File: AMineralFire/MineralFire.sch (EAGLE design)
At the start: 76 parts, among them IC1 LM358, Q1 20MHz, Q2 20MHz, Q3 2N3906, Q4 2N3906, Q5 2N3906, Q6 2N3906, Q7 2N3906, Q8 2N3906, Q9 2N3906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

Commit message: Fixed up reset
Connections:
- new net RST2: ISP2.RST, U2.PC6(/RESET)
- net RST: no longer ISP2.RST, U2.PC6(/RESET)
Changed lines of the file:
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@@
 <label x="55.88" y="68.58" size="1.778" layer="95"/>
-</segment>
-<segment>
-<pinref part="U2" gate="G$1" pin="PC6(/RESET)"/>
-<wire x1="58.42" y1="233.68" x2="50.8" y2="233.68" width="0.1524" layer="91"/>
-<label x="50.8" y="233.68" size="1.778" layer="95"/>
-</segment>
-<segment>
-<pinref part="ISP2" gate="G$1" pin="RST"/>
-<wire x1="-7.62" y1="170.18" x2="-10.16" y2="170.18" width="0.1524" layer="91"/>
-<label x="-10.16" y="170.18" size="1.27" layer="95" rot="R180" xref="yes"/>
 </segment>
 </net>
@@
 </segment>
 </net>
+<net name="RST2" class="0">
+<segment>
+<pinref part="U2" gate="G$1" pin="PC6(/RESET)"/>
+<wire x1="58.42" y1="233.68" x2="50.8" y2="233.68" width="0.1524" layer="91"/>
+<label x="50.8" y="233.68" size="1.778" layer="95"/>
+</segment>
+<segment>
+<pinref part="ISP2" gate="G$1" pin="RST"/>
+<wire x1="-7.62" y1="170.18" x2="-10.16" y2="170.18" width="0.1524" layer="91"/>
+<label x="-10.16" y="170.18" size="1.27" layer="95" rot="R180" xref="yes"/>
+</segment>
+</net>

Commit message: Fixed RST on ISP2 and regulator was wrong way round
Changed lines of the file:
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@@
 <instance part="R11" gate="G$1" x="198.12" y="134.62" rot="R270"/>
 <instance part="R12" gate="G$1" x="187.96" y="134.62" rot="R270"/>
-<instance part="U3" gate="G$1" x="205.74" y="-7.62" rot="MR0"/>
+<instance part="U3" gate="G$1" x="205.74" y="-7.62"/>
 <instance part="C7" gate="G$1" x="220.98" y="-12.7"/>
 <instance part="SUPPLY10" gate="+5V" x="220.98" y="-2.54"/>
@@
 <pinref part="U3" gate="G$1" pin="IN"/>
 <wire x1="220.98" y1="-7.62" x2="220.98" y2="-10.16" width="0.1524" layer="91"/>
-<wire x1="213.36" y1="-7.62" x2="220.98" y2="-7.62" width="0.1524" layer="91"/>
+<wire x1="198.12" y1="-7.62" x2="220.98" y2="-7.62" width="0.1524" layer="91"/>
 <junction x="220.98" y="-7.62"/>
 </segment>
@@
 <pinref part="SUPPLY4" gate="+12V" pin="+12V"/>
 <pinref part="U3" gate="G$1" pin="OUT"/>
-<wire x1="182.88" y1="-7.62" x2="198.12" y2="-7.62" width="0.1524" layer="91"/>
+<wire x1="182.88" y1="-7.62" x2="213.36" y2="-7.62" width="0.1524" layer="91"/>
 <junction x="182.88" y="-7.62"/>
 </segment>
@@
 <segment>
 <pinref part="U2" gate="G$1" pin="PC6(/RESET)"/>
-<wire x1="58.42" y1="233.68" x2="50.8" y2="233.68" width="0.1524" layer="91"/>
-<label x="50.8" y="233.68" size="1.778" layer="95"/>
+<wire x1="58.42" y1="233.68" x2="53.34" y2="233.68" width="0.1524" layer="91"/>
+<label x="53.34" y="233.68" size="1.778" layer="95" rot="R180" xref="yes"/>
 </segment>
 <segment>
 <pinref part="ISP2" gate="G$1" pin="RST"/>
 <wire x1="-7.62" y1="170.18" x2="-10.16" y2="170.18" width="0.1524" layer="91"/>
-<label x="-10.16" y="170.18" size="1.27" layer="95" rot="R180" xref="yes"/>
-</segment>
-</net>
+<label x="-10.16" y="170.18" size="1.778" layer="95" rot="R180" xref="yes"/>
+</segment>
+</net>

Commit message: Fixed RST on ISP2 and regulator was wrong way round
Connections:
- net +12V: now also U3.IN; no longer U3.OUT
- net +5V: now also U3.OUT; no longer U3.IN
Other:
- moved on the sheet: U3
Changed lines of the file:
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@@
 <instance part="R11" gate="G$1" x="198.12" y="134.62" rot="R270"/>
 <instance part="R12" gate="G$1" x="187.96" y="134.62" rot="R270"/>
-<instance part="U3" gate="G$1" x="205.74" y="-7.62"/>
+<instance part="U3" gate="G$1" x="205.74" y="-7.62" rot="MR180"/>
 <instance part="C7" gate="G$1" x="220.98" y="-12.7"/>
 <instance part="SUPPLY10" gate="+5V" x="220.98" y="-2.54"/>
@@
 <pinref part="U3" gate="G$1" pin="GND"/>
 <wire x1="182.88" y1="-20.32" x2="205.74" y2="-20.32" width="0.1524" layer="91"/>
-<wire x1="205.74" y1="-20.32" x2="205.74" y2="-15.24" width="0.1524" layer="91"/>
+<wire x1="205.74" y1="-20.32" x2="205.74" y2="0" width="0.1524" layer="91"/>
 <junction x="182.88" y="-20.32"/>
 <pinref part="C7" gate="G$1" pin="-"/>
@@
 <pinref part="SUPPLY10" gate="+5V" pin="+5V"/>
 <wire x1="220.98" y1="-5.08" x2="220.98" y2="-7.62" width="0.1524" layer="91"/>
-<pinref part="U3" gate="G$1" pin="IN"/>
+<pinref part="U3" gate="G$1" pin="OUT"/>
 <wire x1="220.98" y1="-7.62" x2="220.98" y2="-10.16" width="0.1524" layer="91"/>
-<wire x1="198.12" y1="-7.62" x2="220.98" y2="-7.62" width="0.1524" layer="91"/>
+<wire x1="213.36" y1="-7.62" x2="220.98" y2="-7.62" width="0.1524" layer="91"/>
 <junction x="220.98" y="-7.62"/>
 </segment>
@@
 <junction x="172.72" y="-7.62"/>
 <pinref part="SUPPLY4" gate="+12V" pin="+12V"/>
-<pinref part="U3" gate="G$1" pin="OUT"/>
-<wire x1="182.88" y1="-7.62" x2="213.36" y2="-7.62" width="0.1524" layer="91"/>
+<pinref part="U3" gate="G$1" pin="IN"/>
+<wire x1="182.88" y1="-7.62" x2="198.12" y2="-7.62" width="0.1524" layer="91"/>
 <junction x="182.88" y="-7.62"/>
 </segment>

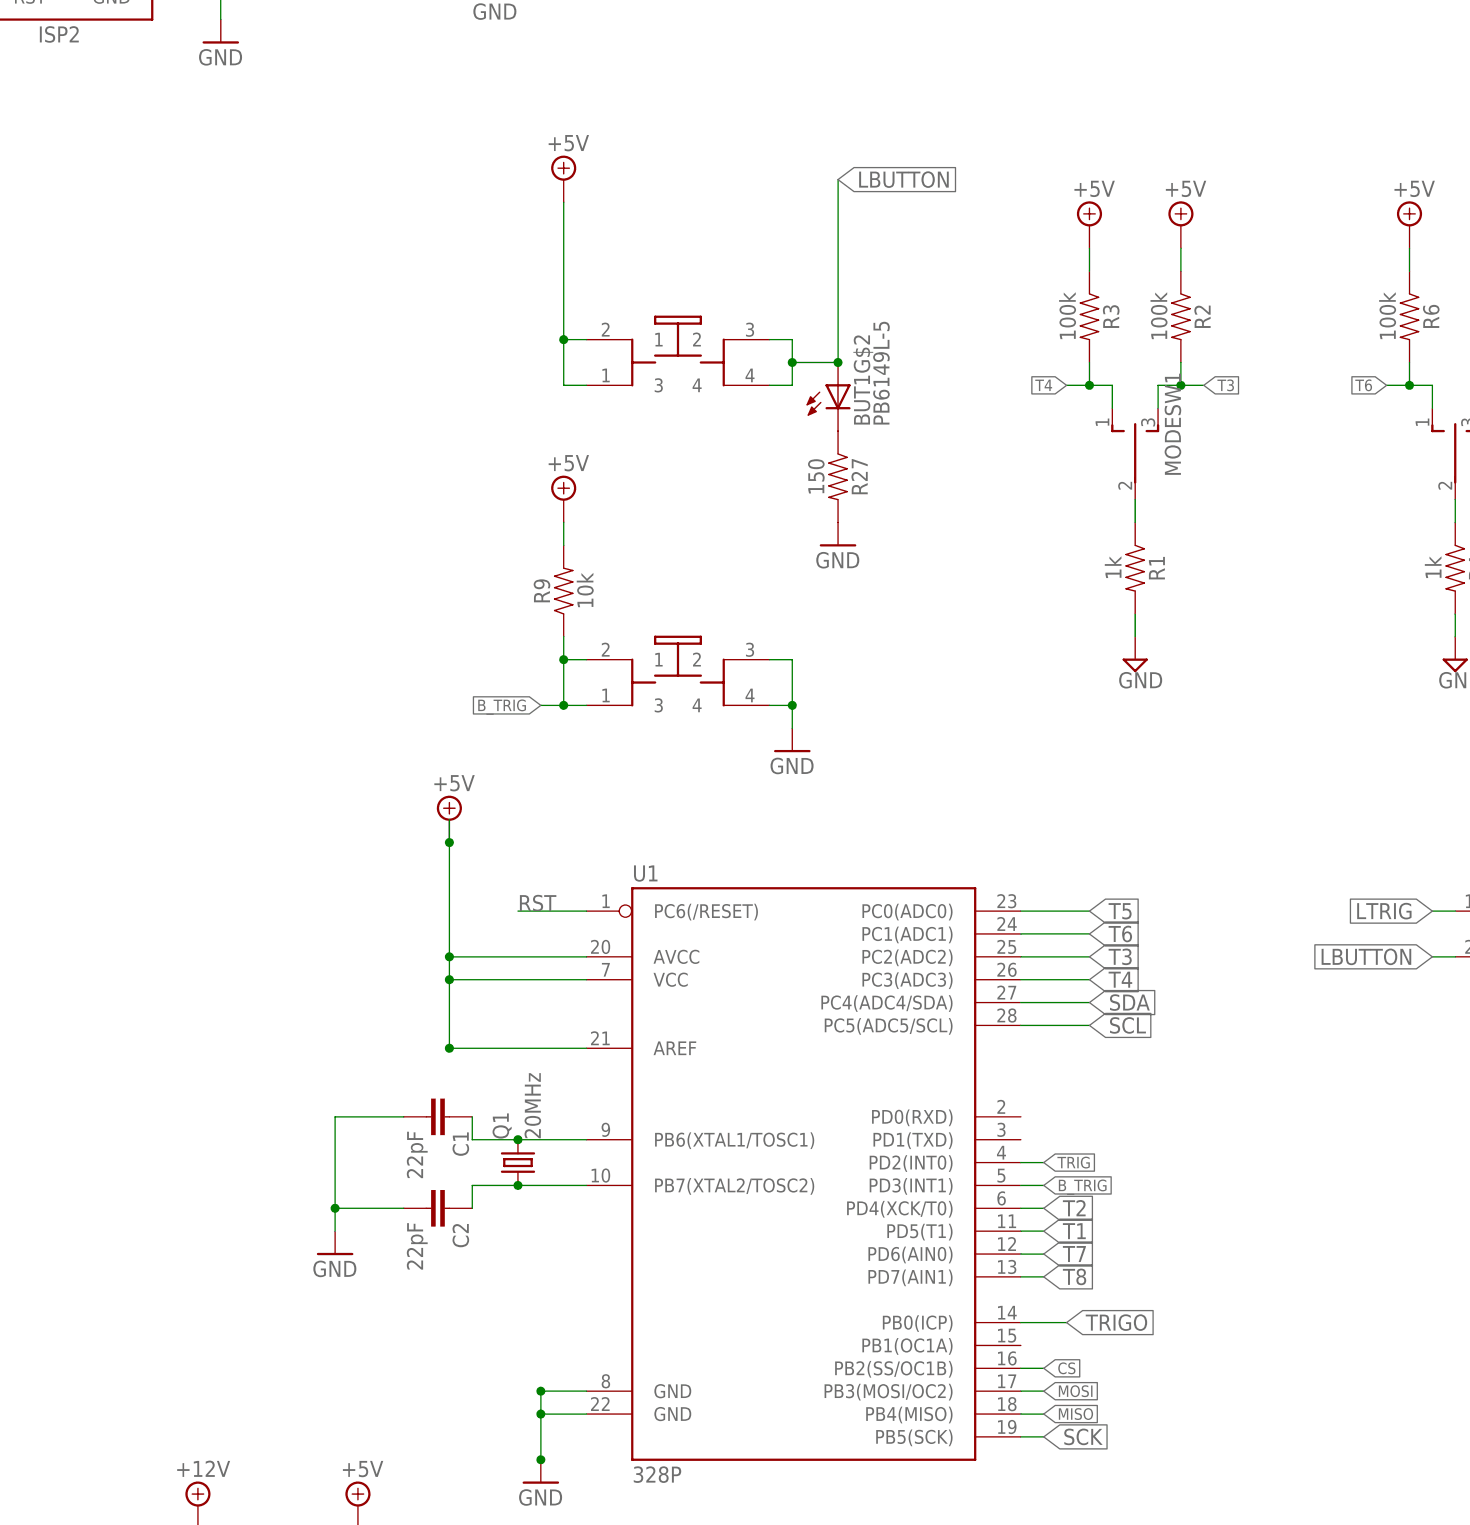
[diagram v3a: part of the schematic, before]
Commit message: changed push button
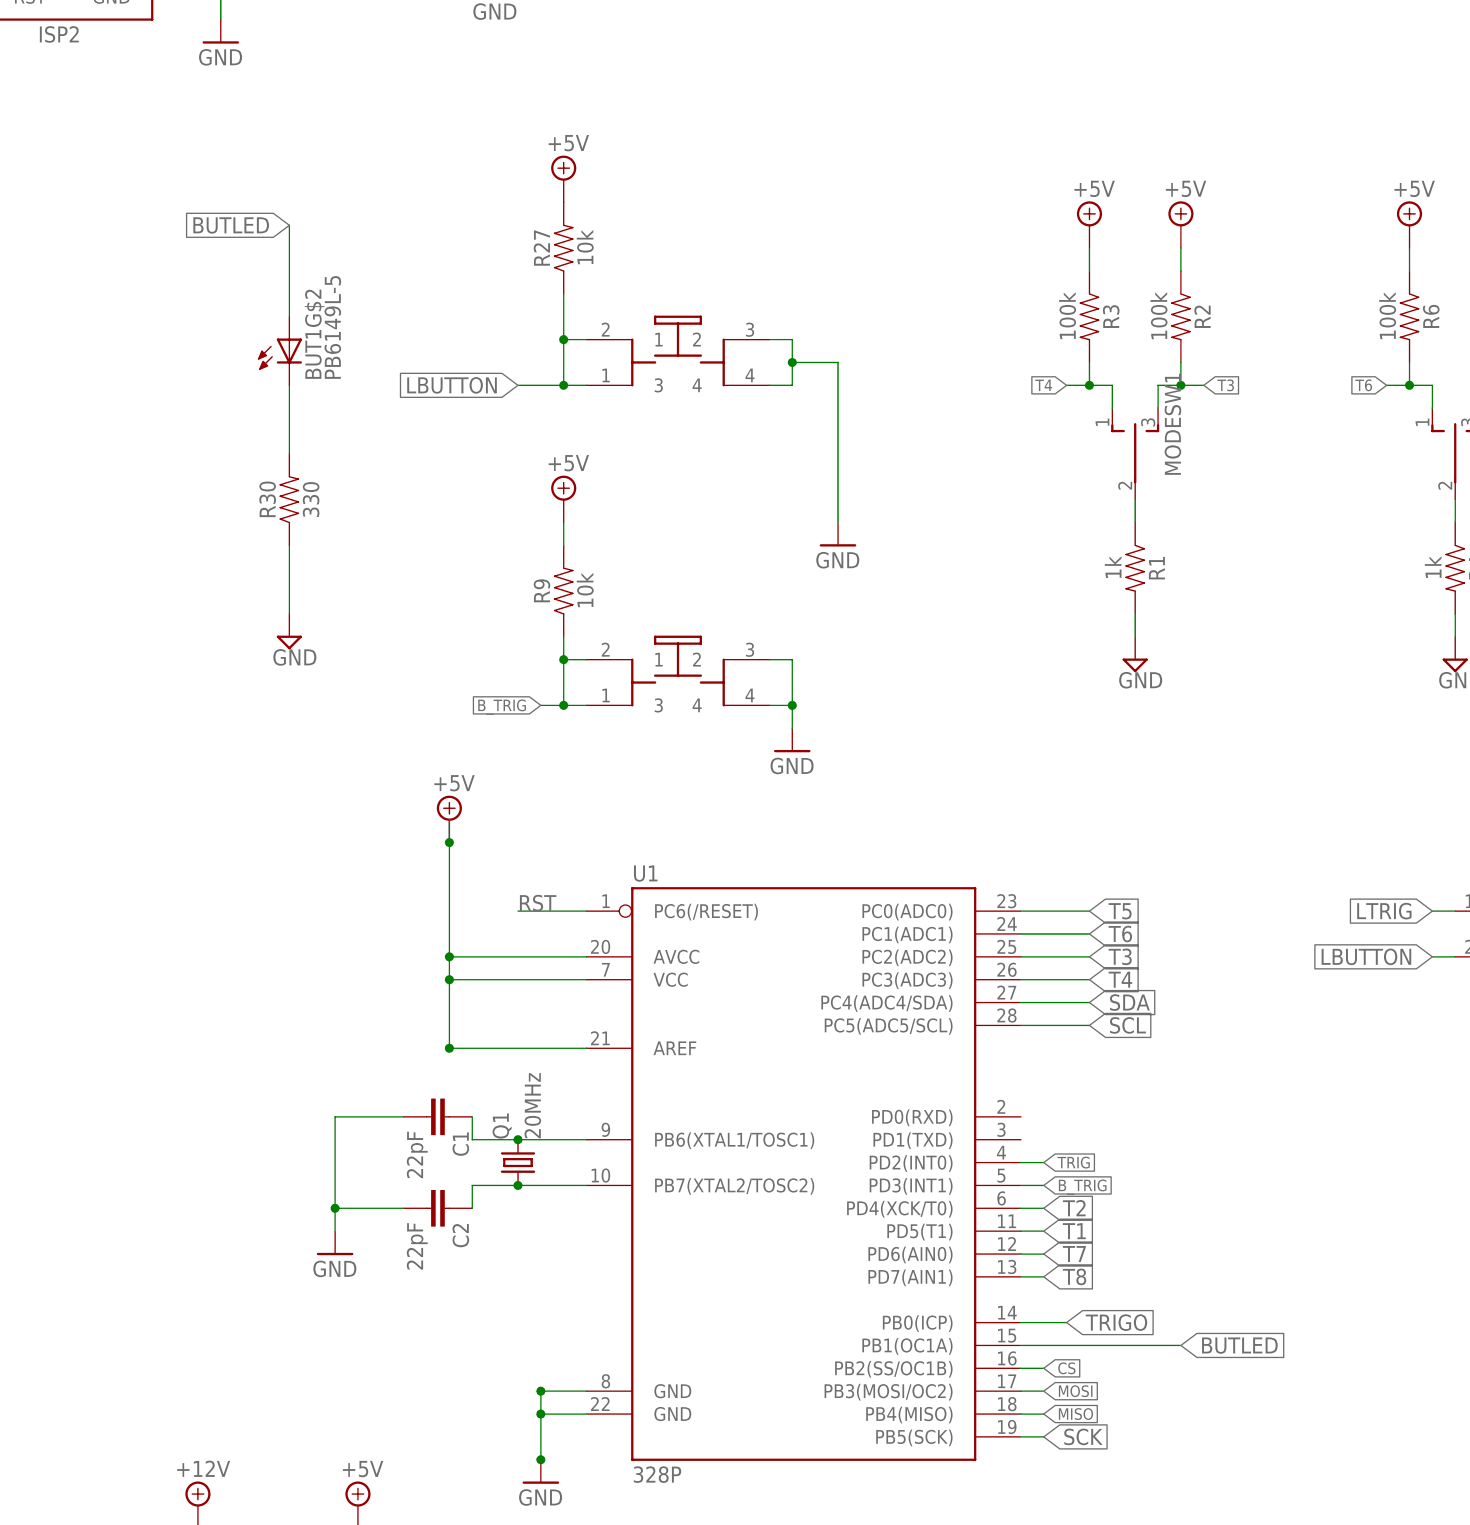
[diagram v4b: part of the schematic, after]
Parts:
- added R30: 330, SparkFun-Resistors:330OHM-HORIZ-1/10W-5%
- R27: value 150 -> 10k; device SparkFun-Resistors:100KOHM-HORIZ-1/4W-5% -> SparkFun-Resistors:10KOHM-HORIZ-1/4W-1%
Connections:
- new net BUTLED: BUT1G$2.A, U1.PB1(OC1A)
- net +5V: now also R27.2; no longer BUT1G$1.1, BUT1G$1.3
- net GND: now also BUT1G$1.2, BUT1G$1.4, R30.1; no longer R27.2
- net LBUTTON: now also BUT1G$1.1, BUT1G$1.3, R27.1; no longer BUT1G$1.2, BUT1G$1.4, BUT1G$2.A
- net N$19: now also R30.2; no longer R27.1
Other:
- moved on the sheet: BUT1G$2, R27
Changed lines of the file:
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@@
 <part name="BUT" library="INSTRUO" deviceset="PB6149L-5" device="" value="PB6149L-5"/>
 <part name="BUT1" library="INSTRUO" deviceset="PB6149L-5" device="" value="PB6149L-5"/>
-<part name="R27" library="SparkFun-Resistors" deviceset="100KOHM" device="-HORIZ-1/4W-5%" value="150"/>
 <part name="V1" library="74ttl-din" deviceset="74*32" device="N"/>
 <part name="SUPPLY28" library="supply2" deviceset="+5V" device=""/>
@@
 <part name="R28" library="SparkFun-Resistors" deviceset="100OHM" device="-HORIZ_KIT-1/4W-1%" value="100"/>
 <part name="R29" library="SparkFun-Resistors" deviceset="100OHM" device="-HORIZ_KIT-1/4W-1%" value="100"/>
+<part name="R27" library="SparkFun-Resistors" deviceset="10KOHM" device="-HORIZ-1/4W-1%" value="10k"/>
+<part name="R30" library="SparkFun-Resistors" deviceset="330OHM" device="-HORIZ-1/10W-5%" value="330"/>
+<part name="SUPPLY41" library="supply2" library_urn="urn:adsk.eagle:library:372" deviceset="GND" device=""/>
 </parts>
 <sheets>
@@
 <instance part="BUT" gate="G$2" x="256.54" y="17.78" rot="R90"/>
 <instance part="BUT1" gate="G$1" x="73.66" y="132.08"/>
-<instance part="BUT1" gate="G$2" x="91.44" y="127"/>
-<instance part="R27" gate="G$1" x="91.44" y="116.84" rot="R270"/>
+<instance part="BUT1" gate="G$2" x="30.48" y="132.08"/>
 <instance part="V1" gate="/1" x="170.18" y="66.04"/>
 <instance part="V1" gate="/+UB" x="203.2" y="73.66"/>
@@
 <instance part="R28" gate="G$1" x="426.72" y="195.58" rot="R90"/>
 <instance part="R29" gate="G$1" x="444.5" y="241.3" rot="R90"/>
+<instance part="R27" gate="G$1" x="60.96" y="142.24" rot="R90"/>
+<instance part="R30" gate="G$1" x="30.48" y="114.3" rot="R90"/>
+<instance part="SUPPLY41" gate="GND" x="30.48" y="99.06"/>
 </instances>
 <busses>
@@
 </segment>
 <segment>
-<pinref part="R27" gate="G$1" pin="2"/>
+<wire x1="83.82" y1="132.08" x2="86.36" y2="132.08" width="0.1524" layer="91"/>
+<wire x1="86.36" y1="132.08" x2="86.36" y2="129.54" width="0.1524" layer="91"/>
+<wire x1="86.36" y1="129.54" x2="86.36" y2="127" width="0.1524" layer="91"/>
+<wire x1="83.82" y1="127" x2="86.36" y2="127" width="0.1524" layer="91"/>
+<pinref part="BUT1" gate="G$1" pin="2"/>
+<pinref part="BUT1" gate="G$1" pin="4"/>
 <pinref part="GND5" gate="1" pin="GND"/>
+<wire x1="86.36" y1="129.54" x2="91.44" y2="129.54" width="0.1524" layer="91"/>
+<wire x1="91.44" y1="129.54" x2="91.44" y2="111.76" width="0.1524" layer="91"/>
+<junction x="86.36" y="129.54"/>
+</segment>
+<segment>
+<pinref part="R30" gate="G$1" pin="1"/>
+<wire x1="30.48" y1="109.22" x2="30.48" y2="101.6" width="0.1524" layer="91"/>
+<pinref part="SUPPLY41" gate="GND" pin="GND"/>
 </segment>
 </net>
@@
 </segment>
 <segment>
-<pinref part="SUPPLY27" gate="+5V" pin="+5V"/>
-<wire x1="60.96" y1="147.32" x2="60.96" y2="132.08" width="0.1524" layer="91"/>
-<wire x1="60.96" y1="132.08" x2="60.96" y2="127" width="0.1524" layer="91"/>
-<wire x1="63.5" y1="127" x2="60.96" y2="127" width="0.1524" layer="91"/>
-<pinref part="BUT1" gate="G$1" pin="3"/>
-<pinref part="BUT1" gate="G$1" pin="1"/>
-<wire x1="60.96" y1="132.08" x2="63.5" y2="132.08" width="0.1524" layer="91"/>
-<junction x="60.96" y="132.08"/>
-</segment>
-<segment>
 <pinref part="Q9" gate="G$1" pin="E"/>
 <wire x1="370.84" y1="294.64" x2="370.84" y2="299.72" width="0.1524" layer="91"/>
@@
 <wire x1="259.08" y1="233.68" x2="259.08" y2="238.76" width="0.1524" layer="91"/>
 <pinref part="SUPPLY40" gate="+5V" pin="+5V"/>
+</segment>
+<segment>
+<pinref part="SUPPLY27" gate="+5V" pin="+5V"/>
+<pinref part="R27" gate="G$1" pin="2"/>
 </segment>
 </net>
@@
 </segment>
 <segment>
-<wire x1="83.82" y1="132.08" x2="86.36" y2="132.08" width="0.1524" layer="91"/>
-<wire x1="86.36" y1="132.08" x2="86.36" y2="129.54" width="0.1524" layer="91"/>
-<wire x1="86.36" y1="129.54" x2="86.36" y2="127" width="0.1524" layer="91"/>
-<wire x1="83.82" y1="127" x2="86.36" y2="127" width="0.1524" layer="91"/>
-<pinref part="BUT1" gate="G$1" pin="2"/>
-<pinref part="BUT1" gate="G$1" pin="4"/>
-<wire x1="86.36" y1="129.54" x2="91.44" y2="129.54" width="0.1524" layer="91"/>
-<junction x="86.36" y="129.54"/>
-<pinref part="BUT1" gate="G$2" pin="A"/>
-<wire x1="91.44" y1="129.54" x2="91.44" y2="149.86" width="0.1524" layer="91"/>
-<junction x="91.44" y="129.54"/>
-<label x="91.44" y="149.86" size="1.778" layer="95" xref="yes"/>
+<pinref part="R27" gate="G$1" pin="1"/>
+<wire x1="60.96" y1="137.16" x2="60.96" y2="132.08" width="0.1524" layer="91"/>
+<pinref part="BUT1" gate="G$1" pin="1"/>
+<wire x1="60.96" y1="132.08" x2="63.5" y2="132.08" width="0.1524" layer="91"/>
+<wire x1="60.96" y1="132.08" x2="60.96" y2="127" width="0.1524" layer="91"/>
+<junction x="60.96" y="132.08"/>
+<pinref part="BUT1" gate="G$1" pin="3"/>
+<wire x1="60.96" y1="127" x2="63.5" y2="127" width="0.1524" layer="91"/>
+<wire x1="60.96" y1="127" x2="55.88" y2="127" width="0.1524" layer="91"/>
+<junction x="60.96" y="127"/>
+<label x="55.88" y="127" size="1.778" layer="95" rot="R180" xref="yes"/>
 </segment>
 </net>
@@
 </segment>
 </net>
-<net name="N$19" class="0">
-<segment>
-<pinref part="BUT1" gate="G$2" pin="C"/>
-<pinref part="R27" gate="G$1" pin="1"/>
-</segment>
-</net>
 <net name="D1" class="0">
 <segment>
@@
 </segment>
 </net>
+<net name="N$19" class="0">
+<segment>
+<pinref part="BUT1" gate="G$2" pin="C"/>
+<pinref part="R30" gate="G$1" pin="2"/>
+<wire x1="30.48" y1="127" x2="30.48" y2="119.38" width="0.1524" layer="91"/>
+</segment>
+</net>
+<net name="BUTLED" class="0">
+<segment>
+<pinref part="U1" gate="G$1" pin="PB1(OC1A)"/>
+<wire x1="111.76" y1="20.32" x2="129.54" y2="20.32" width="0.1524" layer="91"/>
+<label x="129.54" y="20.32" size="1.778" layer="95" xref="yes"/>
+</segment>
+<segment>
+<pinref part="BUT1" gate="G$2" pin="A"/>
+<wire x1="30.48" y1="134.62" x2="30.48" y2="144.78" width="0.1524" layer="91"/>
+<label x="30.48" y="144.78" size="1.778" layer="95" rot="R180" xref="yes"/>
+</segment>
+</net>
